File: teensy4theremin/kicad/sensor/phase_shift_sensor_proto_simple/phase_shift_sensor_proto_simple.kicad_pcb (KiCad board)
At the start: 2 copper layers, 94 x 35.6 mm, 15 parts, among them J1 SENSOR, J2 L_IN, J3 L_OUT, J4 ANT, U1 74HC04, U2 sp721, U3 REG_3V3

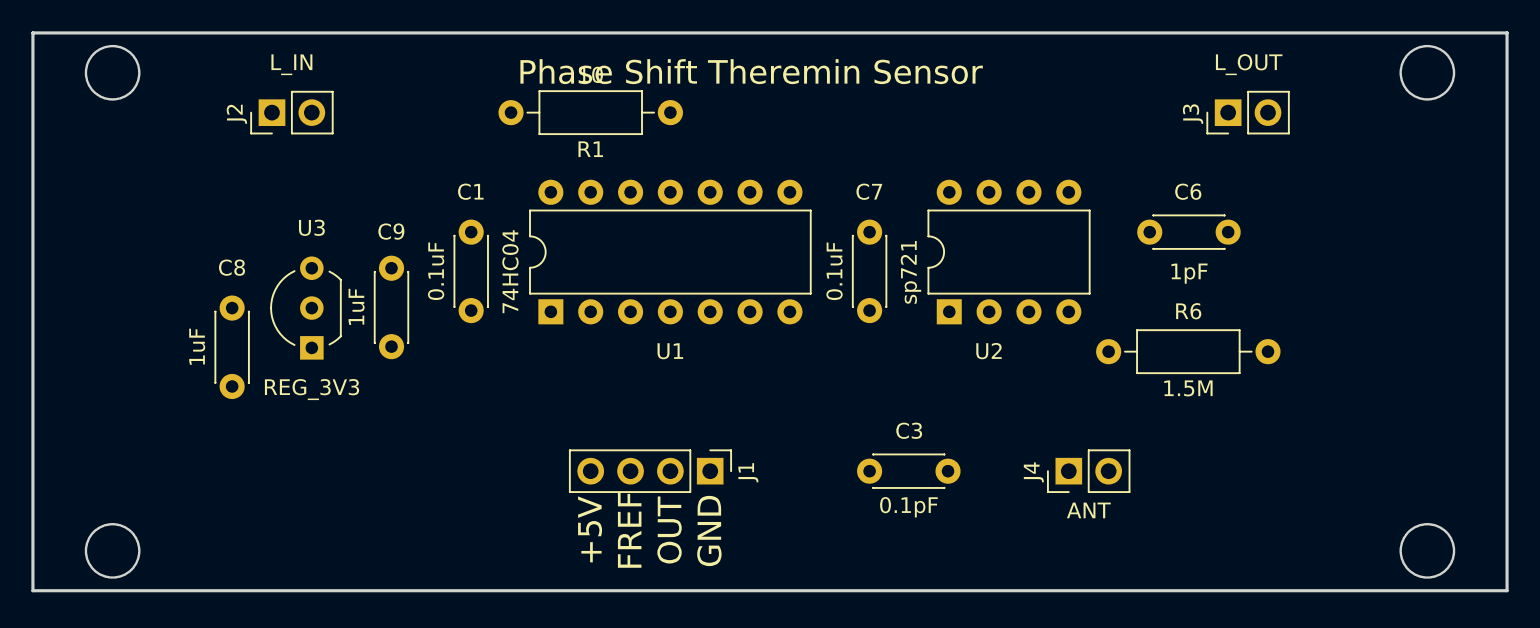
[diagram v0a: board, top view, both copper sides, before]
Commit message: phase shift sensor proto - simple
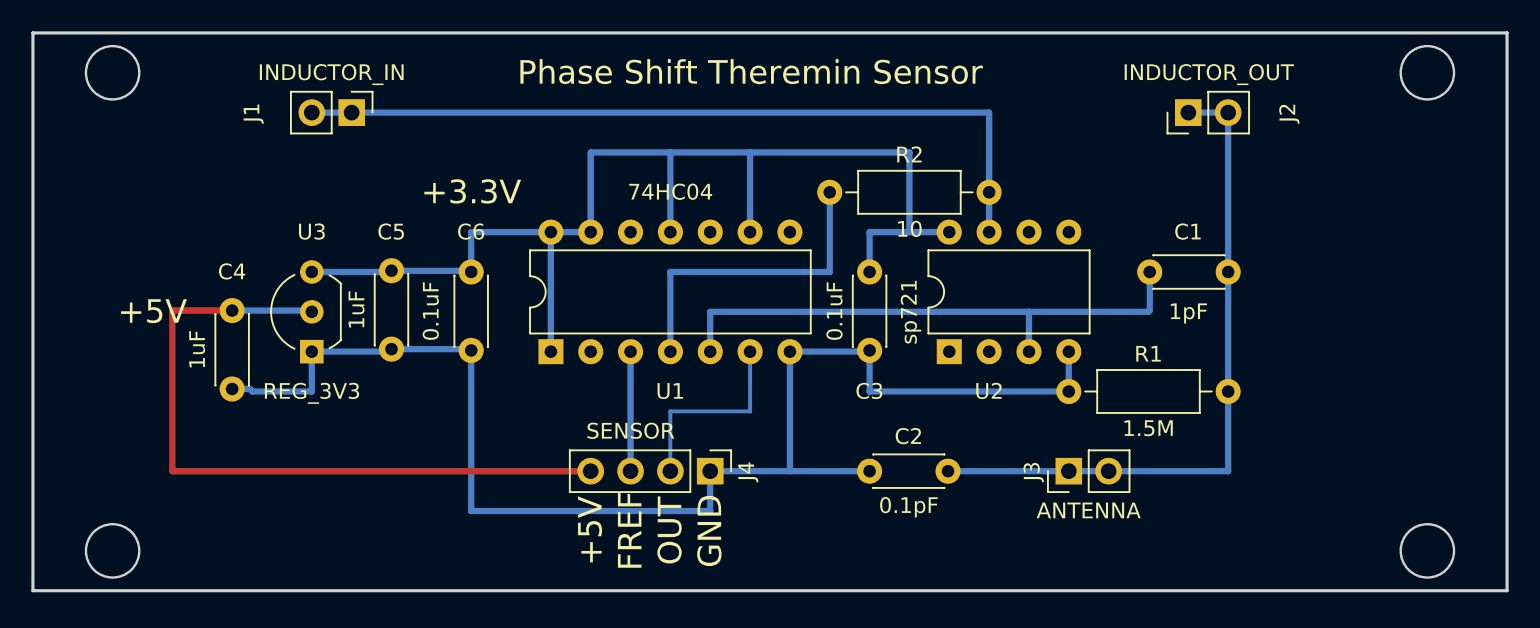
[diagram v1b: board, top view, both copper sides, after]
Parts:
- removed C7: 0.1uF, Capacitor_THT:C_Disc_D4.3mm_W1.9mm_P5.00mm
- removed C8, C9: 1uF, Capacitor_THT:C_Disc_D4.3mm_W1.9mm_P5.00mm
- removed R6: 1.5M, Resistor_THT:R_Axial_DIN0207_L6.3mm_D2.5mm_P10.16mm_Horizontal
- added C2: 0.1pF, Capacitor_THT:C_Disc_D4.3mm_W1.9mm_P5.00mm, F.Cu at (114.3, 114.3)
- added C4: 1uF, Capacitor_THT:C_Disc_D4.3mm_W1.9mm_P5.00mm, F.Cu at (73.7, 104.1)
- added C5: 1uF, Capacitor_THT:C_Disc_D4.3mm_W1.9mm_P5.00mm, F.Cu at (83.8, 101.5)
- added R2: 10, Resistor_THT:R_Axial_DIN0207_L6.3mm_D2.5mm_P10.16mm_Horizontal, F.Cu at (111.8, 96.5)
- C1: value 0.1uF -> 1pF
- C3: value 0.1pF -> 0.1uF
- C6: value 1pF -> 0.1uF
- J1: value SENSOR -> INDUCTOR_IN; footprint Connector_PinHeader_2.54mm:PinHeader_1x04_P2.54mm_Vertical -> Connector_PinHeader_2.54mm:PinHeader_1x02_P2.54mm_Vertical
- J2: value L_IN -> INDUCTOR_OUT
- J3: value L_OUT -> ANTENNA
- J4: value ANT -> SENSOR; footprint Connector_PinHeader_2.54mm:PinHeader_1x02_P2.54mm_Vertical -> Connector_PinHeader_2.54mm:PinHeader_1x04_P2.54mm_Vertical
- R1: value 10 -> 1.5M
- moved J2 58.4 mm to (134.6, 91.4)
- moved C1 48.3 mm to (137.2, 101.6), turned to 180 degrees
- moved C6 48.3 mm to (88.9, 101.6), turned to 270 degrees
- moved J1 32.3 mm to (81.3, 91.4)
- moved R1 31.0 mm to (127.0, 109.2), turned to 0 degrees
- moved J3 25.0 mm to (127.0, 114.3)
- moved J4 22.9 mm to (104.1, 114.3), turned to 270 degrees
- moved C3 12.7 mm to (114.3, 101.6), turned to 270 degrees
- moved U1 2.54 mm to (94.0, 106.7)
- moved U2 2.54 mm to (119.4, 106.7)
- moved U3 0.24 mm to (78.7, 106.7)
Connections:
- C1 pad 1: +3V3 -> Net-(C1-Pad1)
- C1 pad 2: GND -> Net-(C1-Pad2)
- C3 pad 1: GND -> +3V3
- C3 pad 2: Net-(C3-Pad2) -> GND
- C6 pad 1: Net-(C3-Pad2) -> +3V3
- C6 pad 2: Net-(C6-Pad2) -> GND
- J1 pad 1: GND -> Net-(J1-Pad1)
- J1 pad 2: /PWM_OUT -> Net-(J1-Pad1)
- J2 pad 1: Net-(J2-Pad1) -> Net-(C1-Pad1)
- J2 pad 2: Net-(J2-Pad1) -> Net-(C1-Pad1)
- J3 pad 1: Net-(C3-Pad2) -> Net-(C1-Pad1)
- J3 pad 2: Net-(C3-Pad2) -> Net-(C1-Pad1)
- J4 pad 1: Net-(C3-Pad2) -> GND
- J4 pad 2: Net-(C3-Pad2) -> /PWM_OUT
- R1 pad 1: Net-(R1-Pad1) -> GND
- R1 pad 2: Net-(J2-Pad1) -> Net-(C1-Pad1)
- U1 pad 4: Net-(R1-Pad1) -> Net-(R2-Pad1)
- U1 pad 5: Net-(C6-Pad2) -> Net-(C1-Pad2)
- U2 pad 3: Net-(C6-Pad2) -> Net-(C1-Pad2)
- U2 pad 7: Net-(J2-Pad1) -> Net-(J1-Pad1)
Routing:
- net GND: track 0.00 -> 86.9 mm
- net +3V3: track 0.00 -> 76.3 mm
- net Net-(J1-Pad1): track 0.00 -> 50.8 mm
- net +5V: track 0.00 -> 46.1 mm
- net Net-(C1-Pad1): track 0.00 -> 43.3 mm
- net Net-(C1-Pad2): track 0.00 -> 35.6 mm
- net Net-(R2-Pad1): track 0.00 -> 20.3 mm
- net /PWM_OUT: track 0.00 -> 12.7 mm
- net /REF_CLK: track 0.00 -> 7.62 mm
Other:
- board text added: "+3.3V"

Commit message: update schematics
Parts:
- removed R1: 1.5M, Resistor_THT:R_Axial_DIN0207_L6.3mm_D2.5mm_P10.16mm_Horizontal
- added C7: 2.2pF, Capacitor_THT:C_Disc_D4.3mm_W1.9mm_P5.00mm, F.Cu at (139.7, 101.6)
- added R3: 1M, Resistor_THT:R_Axial_DIN0207_L6.3mm_D2.5mm_P10.16mm_Horizontal, F.Cu at (129.5, 96.5)
- added R4: 1M, Resistor_THT:R_Axial_DIN0207_L6.3mm_D2.5mm_P10.16mm_Horizontal, F.Cu at (129.5, 111.8)
- added R5: 100, Resistor_THT:R_Axial_DIN0207_L6.3mm_D2.5mm_P10.16mm_Horizontal, F.Cu at (134.6, 106.7)
- C1: value 1pF -> 2.2pF
- moved J3 10.2 mm to (137.2, 114.3)
- moved C1 9.16 mm to (144.8, 106.7)
- moved C2 5.68 mm to (119.4, 116.8)
- moved C6 2.54 mm to (86.4, 101.6)
- moved J1 2.54 mm to (78.7, 91.4)
- moved J4 2.54 mm to (101.6, 114.3)
- moved R2 2.54 mm to (109.2, 96.5)
- moved U1 2.54 mm to (91.4, 106.7)
- moved C3 2.54 mm to (111.8, 101.6)
- moved C4 2.54 mm to (71.1, 104.1)
- moved C5 2.54 mm to (81.3, 101.5)
- moved U2 2.54 mm to (116.8, 106.7)
- moved U3 2.54 mm to (76.2, 106.7)
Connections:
- U1 pad 5: Net-(C1-Pad2) -> Net-(R3-Pad2)
- U2 pad 3: Net-(C1-Pad2) -> Net-(R3-Pad2)
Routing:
- net Net-(R3-Pad2): track 0.00 -> 45.7 mm
- net Net-(C1-Pad2): track 35.6 -> 5.11 mm
- net +3V3: track 76.3 -> 96.6 mm
- net GND: track 86.9 -> 104.7 mm
- net Net-(C1-Pad1): track 43.3 -> 56.0 mm
- net Net-(C7-Pad2): track 0.00 -> 5.11 mm

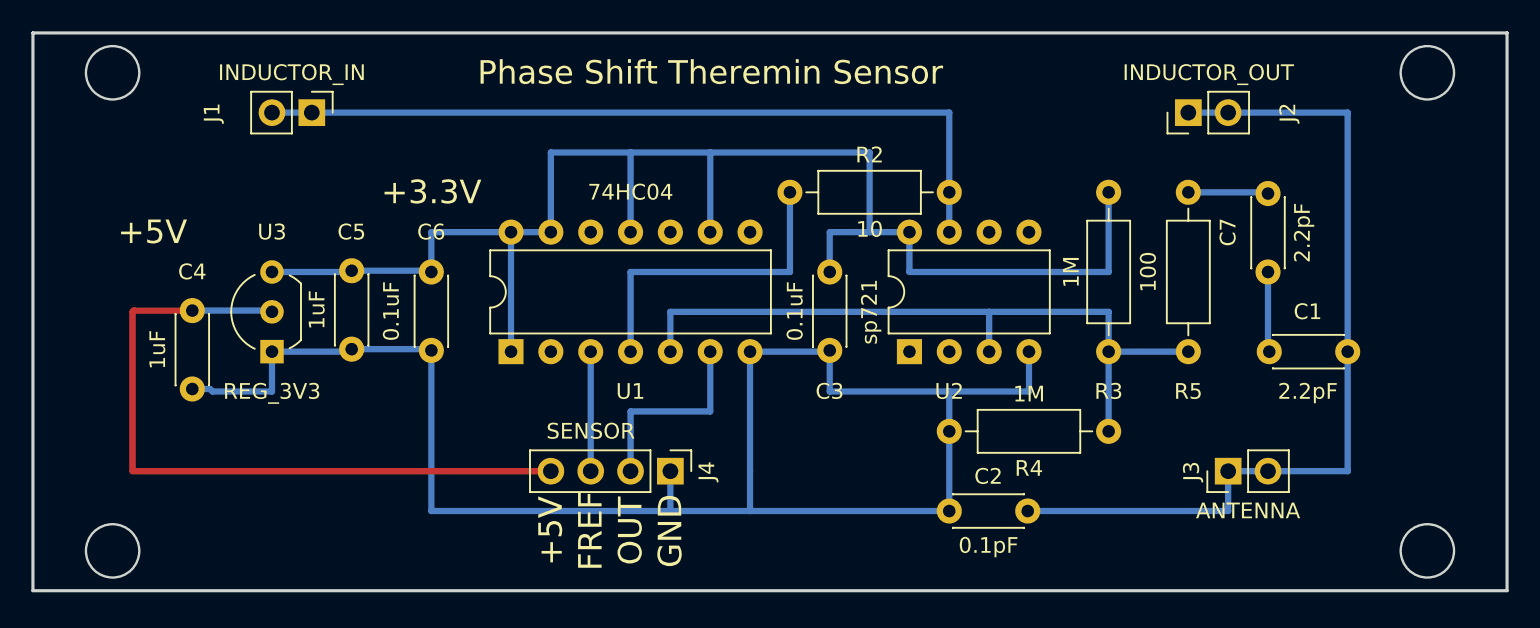
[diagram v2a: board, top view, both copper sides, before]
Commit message: update phase shift sensor schematics
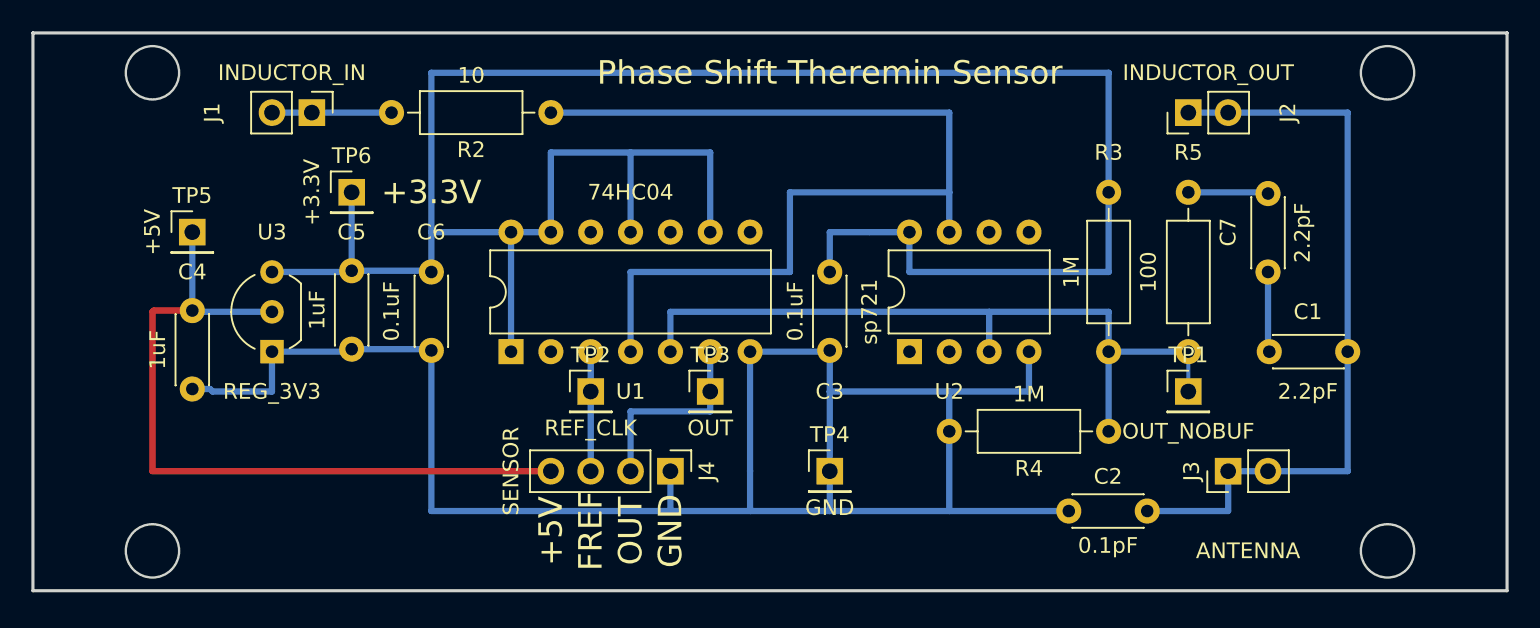
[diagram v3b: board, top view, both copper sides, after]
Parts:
- added TP1: OUT_NOBUF, Connector_PinHeader_2.54mm:PinHeader_1x01_P2.54mm_Vertical, F.Cu at (134.6, 109.2)
- added TP2: REF_CLK, Connector_PinHeader_2.54mm:PinHeader_1x01_P2.54mm_Vertical, F.Cu at (96.5, 109.2)
- added TP3: OUT, Connector_PinHeader_2.54mm:PinHeader_1x01_P2.54mm_Vertical, F.Cu at (104.1, 109.2)
- added TP4: GND, Connector_PinHeader_2.54mm:PinHeader_1x01_P2.54mm_Vertical, F.Cu at (111.8, 114.3)
- added TP5: +5V, Connector_PinHeader_2.54mm:PinHeader_1x01_P2.54mm_Vertical, F.Cu at (71.1, 99.1)
- added TP6: +3.3V, Connector_PinHeader_2.54mm:PinHeader_1x01_P2.54mm_Vertical, F.Cu at (81.3, 96.5)
- moved R2 16.1 mm to (94.0, 91.4), turned to 180 degrees
- moved C2 7.62 mm to (127.0, 116.8)
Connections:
- net /PWM_OUT renamed /OUT
- U2 pad 7: Net-(J1-Pad1) -> Net-(R2-Pad1)
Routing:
- net +3V3: track 96.6 -> 147.3 mm
- net Net-(J1-Pad1): track 50.8 -> 7.62 mm
- net Net-(R2-Pad1): track 20.3 -> 63.5 mm
- net GND: track 104.7 -> 119.9 mm
- net Net-(C1-Pad1): track 56.0 -> 48.3 mm
- net Net-(R3-Pad2): track 45.7 -> 48.3 mm
- net +5V: track 46.1 -> 48.2 mm
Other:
- outline, holes or cut-outs redrawn

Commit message: update sensor schematic
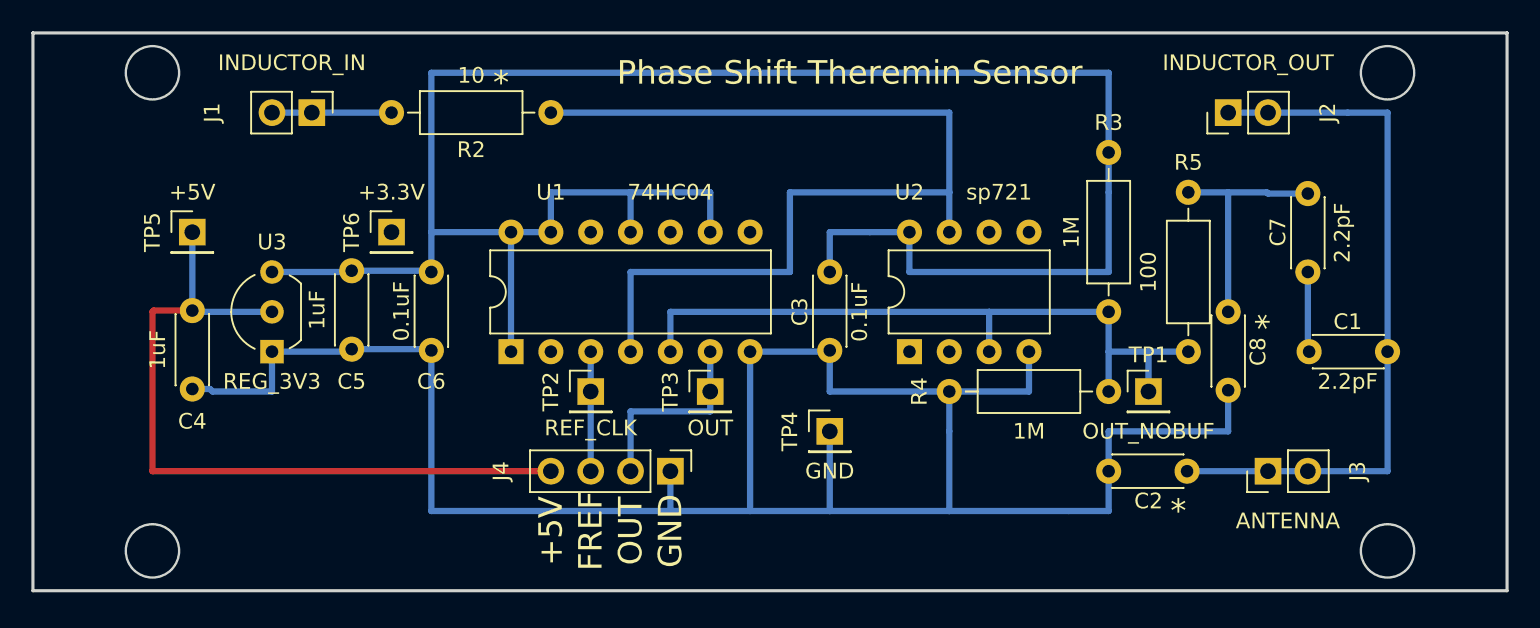
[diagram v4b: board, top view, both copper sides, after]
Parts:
- added C8: 6.8pF, Capacitor_THT:C_Disc_D4.3mm_W1.9mm_P5.00mm, F.Cu at (137.2, 104.1)
- moved C2 3.59 mm to (129.5, 114.3)
- moved TP6 3.59 mm to (83.8, 99.1)
- moved C7 2.54 mm to (142.2, 101.6)
- moved R4 2.54 mm to (129.5, 109.2)
- moved C1 2.54 mm to (147.3, 106.7)
- moved J2 2.54 mm to (137.2, 91.4)
- moved J3 2.54 mm to (139.7, 114.3)
- moved R3 2.54 mm to (129.5, 94.0)
- moved TP1 2.54 mm to (132.1, 109.2)
- moved TP4 2.54 mm to (111.8, 111.8)
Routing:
- net GND: track 119.9 -> 135.3 mm
- net +3V3: track 147.3 -> 134.7 mm
- net Net-(C7-Pad2): track 5.11 -> 15.3 mm
- net Net-(R3-Pad2): track 48.3 -> 45.7 mm
- net Net-(C1-Pad1): track 48.3 -> 45.8 mm
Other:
- board text added: "*"
- board text removed: "+3.3V"

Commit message: update phase shift sensor prototype PCB
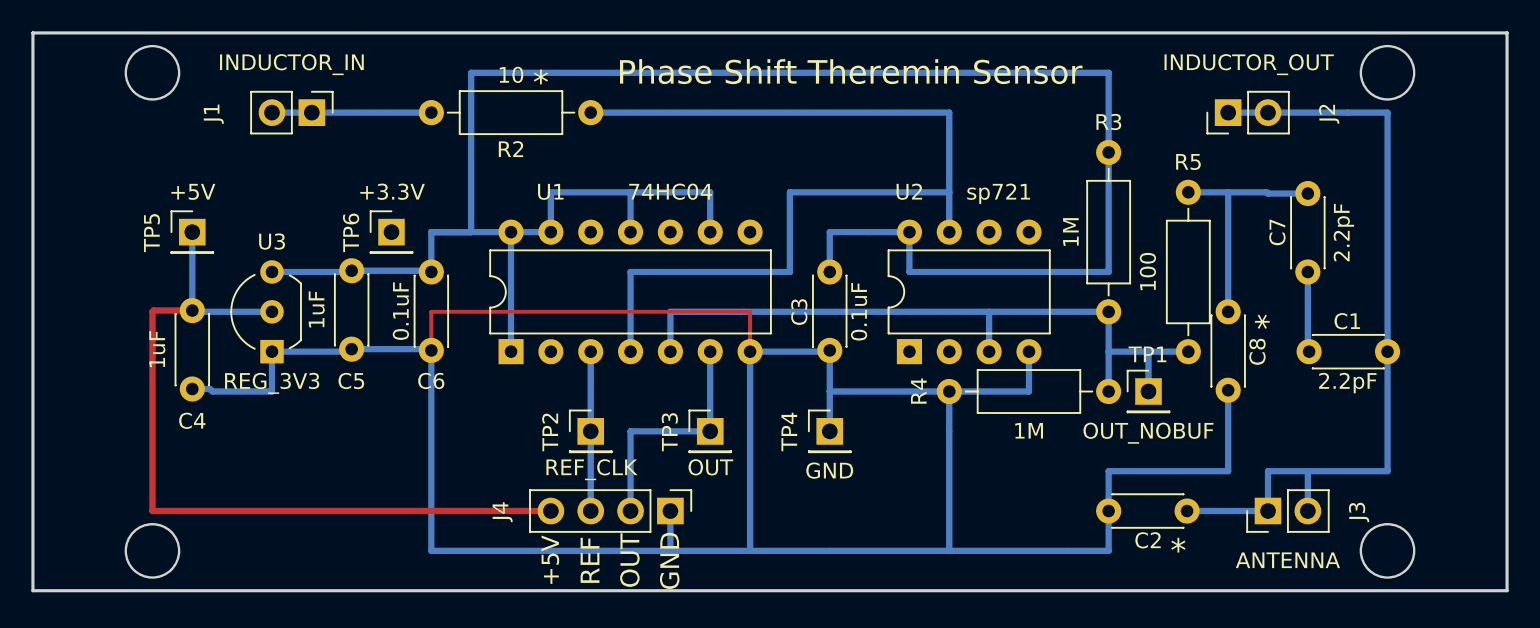
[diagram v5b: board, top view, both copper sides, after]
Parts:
- moved C2 2.54 mm to (129.5, 116.8)
- moved J3 2.54 mm to (139.7, 116.8)
- moved J4 2.54 mm to (101.6, 116.8)
- moved TP2 2.54 mm to (96.5, 111.8)
- moved TP3 2.54 mm to (104.1, 111.8)
- moved R2 2.54 mm to (96.5, 91.4)
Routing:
- net GND: track 135.3 -> 168.2 mm
- net Net-(C1-Pad1): track 45.8 -> 50.9 mm
- net Net-(J1-Pad1): track 7.62 -> 10.2 mm
- net /REF_CLK: track 7.62 -> 10.2 mm
- net /OUT: track 12.7 -> 15.2 mm
- net +5V: track 48.2 -> 50.8 mm
- net Net-(R2-Pad1): track 63.5 -> 61.0 mm
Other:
- board text added: "REF"
- board text removed: "FREF"
